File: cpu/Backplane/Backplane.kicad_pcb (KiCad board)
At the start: 2 copper layers, 162 parts, among them J1 GPR A1, J10 SI 2, J11 DI 1, J12 DI 2, J13 SP 1, J14 SP 2, J15 PC 1, J16 PC 2, J17 HOLDING 1, J18 HOLDING 2, J2 GPR A2, J3 GPR B1, J4 GPR B2, J5 GPR C1, J6 GPR C2, J7 GPR D1, J8 GPR D2, J9 SI 1, U1 74LS245, U2 74LS245, U3 74LS245, U4 74LS245, U5 74LS245, U6 74LS245, U7 74LS245, U8 74LS245

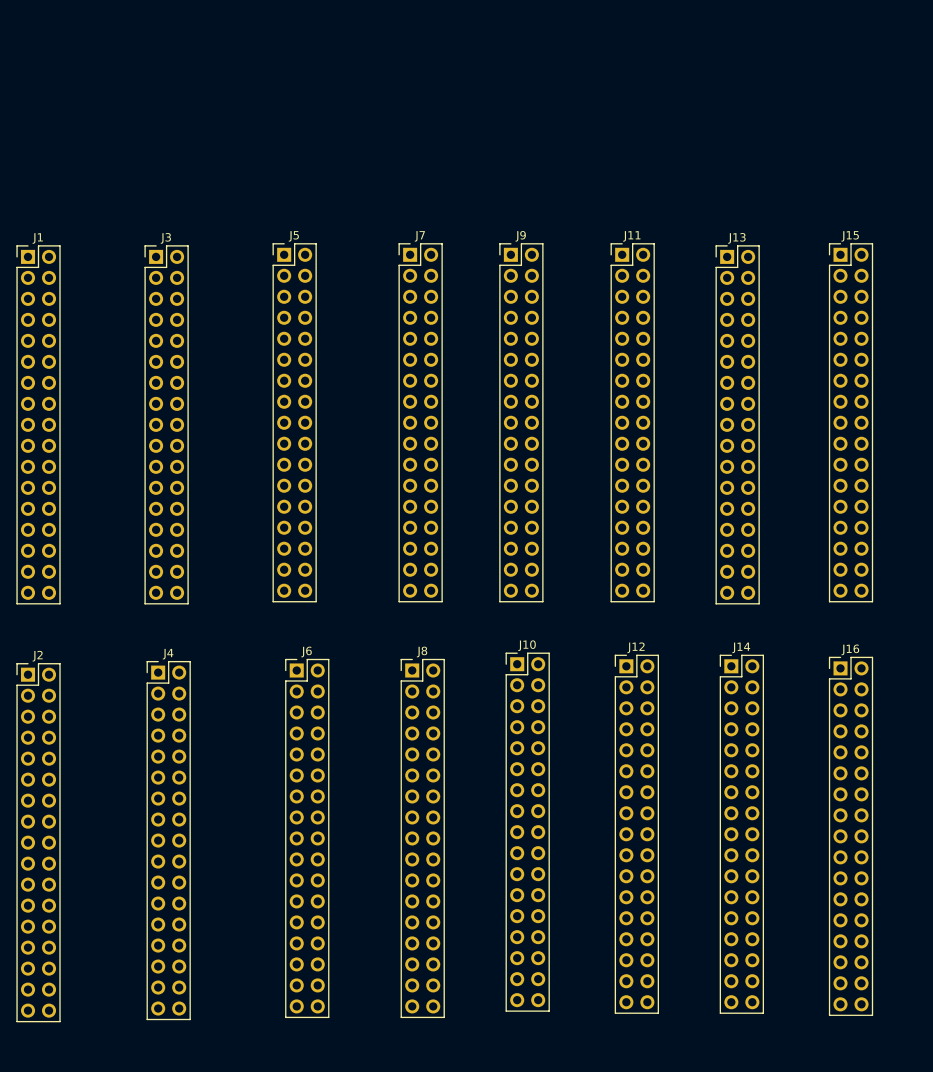
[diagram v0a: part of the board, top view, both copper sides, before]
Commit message: Added missing power pins to GPR
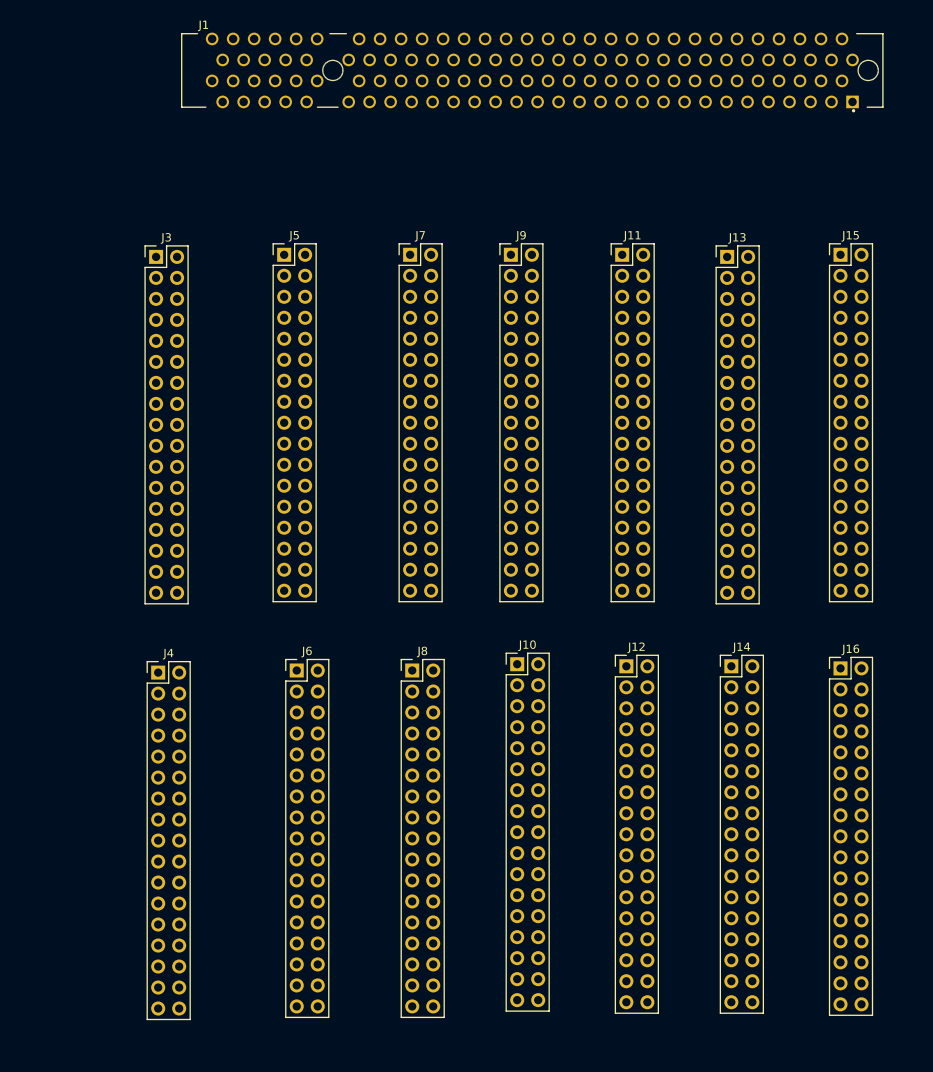
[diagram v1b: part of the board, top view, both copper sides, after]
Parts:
- removed J2: GPR A2, Connector_PinHeader_2.54mm:PinHeader_2x17_P2.54mm_Vertical
- J1: value GPR A1 -> GPR_A; footprint Connector_PinHeader_2.54mm:PinHeader_2x17_P2.54mm_Vertical -> TE-PCI-32bit:TE_1-5145154-2
- moved J1 65.1 mm to (88.7, 0.30)
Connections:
- J1 pad 1: /d_bus_read_gpr_a -> (no net)
- J1 pad 10: /d_bus_04 -> (no net)
- J1 pad 11: Net-(J1-Pad11) -> (no net)
- J1 pad 12: /d_bus_05 -> (no net)
- J1 pad 13: Net-(J1-Pad13) -> (no net)
- J1 pad 14: /d_bus_06 -> (no net)
- J1 pad 15: Net-(J1-Pad15) -> (no net)
- J1 pad 16: /d_bus_07 -> (no net)
- J1 pad 17: Net-(J1-Pad17) -> (no net)
- J1 pad 18: /d_bus_08 -> (no net)
- J1 pad 19: Net-(J1-Pad19) -> (no net)
- J1 pad 2: /d_bus_00 -> (no net)
- J1 pad 20: /d_bus_09 -> (no net)
- J1 pad 21: Net-(J1-Pad21) -> (no net)
- J1 pad 22: /d_bus_10 -> (no net)
- J1 pad 23: /RST -> (no net)
- J1 pad 24: /d_bus_11 -> (no net)
- J1 pad 25: /DBG -> (no net)
- J1 pad 26: /d_bus_12 -> (no net)
- J1 pad 27: /HLT -> (no net)
- J1 pad 28: /d_bus_13 -> (no net)
- J1 pad 29: /~CLK -> (no net)
- J1 pad 3: /d_bus_write_gpr_a -> (no net)
- J1 pad 30: /d_bus_14 -> (no net)
- J1 pad 31: /CLK -> (no net)
- J1 pad 32: /d_bus_15 -> (no net)
- J1 pad 33: GND -> (no net)
- J1 pad 34: +5V -> (no net)
- J1 pad 4: /d_bus_01 -> (no net)
- J1 pad 5: /x_bus_write_gpr_a -> (no net)
- J1 pad 6: /d_bus_02 -> (no net)
- J1 pad 7: /y_bus_write_gpr_a -> (no net)
- J1 pad 8: /d_bus_03 -> (no net)
- J1 pad 9: Net-(J1-Pad9) -> (no net)
- J11 pad 25: /DBG -> /~DBG
- J13 pad 25: /DBG -> /~DBG
- J15 pad 25: /DBG -> /~DBG
- J3 pad 25: /DBG -> /~DBG
- J5 pad 25: /DBG -> /~DBG
- J7 pad 25: /DBG -> /~DBG
- J9 pad 25: /DBG -> /~DBG
- U1 pad 19: /DBG -> /~DBG
- U2 pad 19: /DBG -> /~DBG
- U3 pad 19: /DBG -> /~DBG
- U4 pad 19: /DBG -> /~DBG
- U5 pad 19: /DBG -> /~DBG
- U6 pad 19: /DBG -> /~DBG
- U7 pad 19: /DBG -> /~DBG
- U8 pad 19: /DBG -> /~DBG

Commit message: Upgrade to KiCad 6 and commit a bunch of random stuff
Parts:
- removed R0, R1, R10, R11, R12, R13, R14, R15, R16, R17, R18, R19, R2, R20, R21, R22, R23, R24, R25, R26, R27, R28, R29, R3, R30, R31, R32, R33, R34, R35, R36, R37, R38, R39, R4, R40, R41, R42, R43, R44, R45, R46, R47, R48, R49, R5, R50, R51, R52, R53, R54, R55, R56, R57, R58, R59, R6, R60, R61, R62, R63, R7, R8, R9: 220R, Resistor_SMD:R_0603_1608Metric_Pad1.05x0.95mm_HandSolder
- added C10: 47uF, Capacitor_SMD:CP_Elec_4x5.4, F.Cu at (193.0, 191.2)
- added C11: 47uF, Capacitor_SMD:CP_Elec_4x5.4, F.Cu at (193.0, 171.0)
- added C12: 47uF, Capacitor_SMD:CP_Elec_4x5.4, F.Cu at (193.0, 151.0)
- added C13: 47uF, Capacitor_SMD:CP_Elec_4x5.4, F.Cu at (193.0, 131.0)
- added C14: 47uF, Capacitor_SMD:CP_Elec_4x5.4, F.Cu at (193.0, 111.0)
- added C15: 47uF, Capacitor_SMD:CP_Elec_4x5.4, F.Cu at (193.0, 91.0)
- added C16: 47uF, Capacitor_SMD:CP_Elec_4x5.4, F.Cu at (193.0, 71.0)
- added C17: 47uF, Capacitor_SMD:CP_Elec_4x5.4, F.Cu at (193.0, 51.0)
- added C18: 47uF, Capacitor_SMD:CP_Elec_4x5.4, F.Cu at (62.5, 191.0)
- added C19: 47uF, Capacitor_SMD:CP_Elec_4x5.4, F.Cu at (62.5, 171.0)
- added C20: 47uF, Capacitor_SMD:CP_Elec_4x5.4, F.Cu at (62.5, 151.0)
- added C21: 47uF, Capacitor_SMD:CP_Elec_4x5.4, F.Cu at (62.5, 111.0)
- added C22: 47uF, Capacitor_SMD:CP_Elec_4x5.4, F.Cu at (62.5, 91.0)
- added C23: 47uF, Capacitor_SMD:CP_Elec_4x5.4, F.Cu at (62.5, 71.0)
- added C24: 47uF, Capacitor_SMD:CP_Elec_4x5.4, F.Cu at (62.5, 51.0)
- added C25: 47uF, Capacitor_SMD:CP_Elec_4x5.4, F.Cu at (70.5, 36.1)
- added C9: 0.1uF, Capacitor_SMD:C_0603_1608Metric_Pad1.05x0.95mm_HandSolder, F.Cu at (83.2, 28.4)
- added D64: D_Zener, Diode_THT:D_A-405_P10.16mm_Horizontal, F.Cu at (75.3, 37.4)
- added J19: Conn_01x04_Female, Connector_PinHeader_2.54mm:PinHeader_1x04_P2.54mm_Vertical, F.Cu at (213.3, 28.4)
- added J2: GPR_B, TE-PCI-32bit:TE_1-5145154-2, F.Cu at (241.4, 171.1)
- added J20: Conn_01x07_Female, Connector_PinHeader_2.54mm:PinHeader_1x07_P2.54mm_Vertical, F.Cu at (194.6, 28.4)
- added J21: Conn_01x07_Female, Connector_PinHeader_2.54mm:PinHeader_1x07_P2.54mm_Vertical, F.Cu at (168.2, 28.4)
- added J22: Conn_01x07_Female, Connector_PinHeader_2.54mm:PinHeader_1x07_P2.54mm_Vertical, F.Cu at (141.9, 28.4)
- added J23: Conn_01x07_Female, Connector_PinHeader_2.54mm:PinHeader_1x07_P2.54mm_Vertical, F.Cu at (115.5, 28.4)
- added J24: Conn_01x05_Female, Connector_PinHeader_2.54mm:PinHeader_1x05_P2.54mm_Vertical, F.Cu at (36.0, 199.9)
- added J25: Barrel_Jack, digikey-footprints:Barrel_Jack_5.5mmODx2.1mmID_PJ-202A, F.Cu at (62.5, 36.4)
- added J27: Conn_01x04_Female, Connector_PinHeader_2.54mm:PinHeader_1x04_P2.54mm_Vertical, F.Cu at (36.0, 154.7)
- added J28: Conn_01x14_Female, Connector_PinHeader_2.54mm:PinHeader_1x14_P2.54mm_Vertical, F.Cu at (36.0, 193.7)
- added J29: IO_1, TE-PCI-32bit:TE_1-5145154-2, F.Cu at (111.0, 111.1)
- added J30: IO_2, TE-PCI-32bit:TE_1-5145154-2, F.Cu at (111.0, 91.1)
- added J31: IO_3, TE-PCI-32bit:TE_1-5145154-2, F.Cu at (111.0, 71.1)
- added J32: IO_4, TE-PCI-32bit:TE_1-5145154-2, F.Cu at (111.0, 51.1)
- added RN1: 220R, Resistor_SMD:R_Array_Convex_8x0602, F.Cu at (88.3, 247.5)
- added RN2: 220R, Resistor_SMD:R_Array_Convex_8x0602, F.Cu at (50.7, 245.6)
- added RN3: 220R, Resistor_SMD:R_Array_Convex_8x0602, F.Cu at (217.9, 249.1)
- added RN4: 220R, Resistor_SMD:R_Array_Convex_8x0602, F.Cu at (187.7, 249.1)
- added RN5: 220R, Resistor_SMD:R_Array_Convex_8x0602, F.Cu at (282.1, 248.7)
- added RN6: 220R, Resistor_SMD:R_Array_Convex_8x0602, F.Cu at (250.3, 248.7)
- added RN7: 220R, Resistor_SMD:R_Array_Convex_8x0602, F.Cu at (154.3, 248.7)
- added RN8: 220R, Resistor_SMD:R_Array_Convex_8x0602, F.Cu at (122.0, 248.4)
- added U10: 74LS04, Package_SO:SOIC-14_3.9x8.7mm_P1.27mm, F.Cu at (81.6, 34.0)
- added U9: MCP100-450D, digikey-footprints:SOT-23-3, F.Cu at (70.5, 28.3)
- J10: value SI 2 -> ALU; footprint Connector_PinHeader_2.54mm:PinHeader_2x17_P2.54mm_Vertical -> TE-PCI-32bit:TE_1-5145154-2
- J11: value DI 1 -> Memory; footprint Connector_PinHeader_2.54mm:PinHeader_2x17_P2.54mm_Vertical -> TE-PCI-32bit:TE_1-5145154-2
- J12: value DI 2 -> Conn_01x16_Female; footprint Connector_PinHeader_2.54mm:PinHeader_2x17_P2.54mm_Vertical -> Connector_PinHeader_2.54mm:PinHeader_1x16_P2.54mm_Vertical
- J13: value SP 1 -> Conn_01x16_Female; footprint Connector_PinHeader_2.54mm:PinHeader_2x17_P2.54mm_Vertical -> Connector_PinHeader_2.54mm:PinHeader_1x16_P2.54mm_Vertical
- J14: value SP 2 -> Conn_01x16_Female; footprint Connector_PinHeader_2.54mm:PinHeader_2x17_P2.54mm_Vertical -> Connector_PinHeader_2.54mm:PinHeader_1x16_P2.54mm_Vertical
- J15: value PC 1 -> Conn_01x16_Female; footprint Connector_PinHeader_2.54mm:PinHeader_2x17_P2.54mm_Vertical -> Connector_PinHeader_2.54mm:PinHeader_1x16_P2.54mm_Vertical
- J16: value PC 2 -> Conn_01x04_Female; footprint Connector_PinHeader_2.54mm:PinHeader_2x17_P2.54mm_Vertical -> Connector_PinHeader_2.54mm:PinHeader_1x04_P2.54mm_Vertical
- J17: value HOLDING 1 -> Conn_01x04_Female; footprint Connector_PinHeader_2.54mm:PinHeader_2x17_P2.54mm_Vertical -> Connector_PinHeader_2.54mm:PinHeader_1x04_P2.54mm_Vertical
- J18: value HOLDING 2 -> Conn_01x04_Female; footprint Connector_PinHeader_2.54mm:PinHeader_2x17_P2.54mm_Vertical -> Connector_PinHeader_2.54mm:PinHeader_1x04_P2.54mm_Vertical
- J3: value GPR B1 -> GPR_C; footprint Connector_PinHeader_2.54mm:PinHeader_2x17_P2.54mm_Vertical -> TE-PCI-32bit:TE_1-5145154-2
- J4: value GPR B2 -> GPR_D; footprint Connector_PinHeader_2.54mm:PinHeader_2x17_P2.54mm_Vertical -> TE-PCI-32bit:TE_1-5145154-2
- J5: value GPR C1 -> AReg_PC; footprint Connector_PinHeader_2.54mm:PinHeader_2x17_P2.54mm_Vertical -> TE-PCI-32bit:TE_1-5145154-2
- J6: value GPR C2 -> AReg_SP; footprint Connector_PinHeader_2.54mm:PinHeader_2x17_P2.54mm_Vertical -> TE-PCI-32bit:TE_1-5145154-2
- J7: value GPR D1 -> AReg_SI; footprint Connector_PinHeader_2.54mm:PinHeader_2x17_P2.54mm_Vertical -> TE-PCI-32bit:TE_1-5145154-2
- J8: value GPR D2 -> AReg_DI; footprint Connector_PinHeader_2.54mm:PinHeader_2x17_P2.54mm_Vertical -> TE-PCI-32bit:TE_1-5145154-2
- J9: value SI 1 -> Pipeline; footprint Connector_PinHeader_2.54mm:PinHeader_2x17_P2.54mm_Vertical -> TE-PCI-32bit:TE_1-5145154-2
- moved D15 290.5 mm to (45.9, 254.7)
- moved D14 290.0 mm to (49.7, 254.7)
- moved D13 289.4 mm to (53.5, 254.7)
- moved D12 288.9 mm to (57.3, 254.7)
- moved D11 288.4 mm to (61.1, 254.7)
- moved D10 287.9 mm to (64.9, 254.7)
- moved D9 287.4 mm to (68.7, 254.7)
- moved D8 286.8 mm to (72.5, 254.7)
- moved U1 286.4 mm to (86.5, 238.9)
- moved D7 286.3 mm to (76.3, 254.7)
- moved D6 285.8 mm to (80.1, 254.7)
- moved U2 285.7 mm to (61.5, 238.9)
- moved D5 285.3 mm to (83.9, 254.7)
- moved D4 284.8 mm to (87.7, 254.7)
- moved D3 284.3 mm to (91.5, 254.7)
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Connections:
- D0 pad 1: Net-(D0-Pad1) -> GND
- D1 pad 1: Net-(D1-Pad1) -> GND
- D10 pad 1: Net-(D10-Pad1) -> GND
- D11 pad 1: Net-(D11-Pad1) -> GND
- D12 pad 1: Net-(D12-Pad1) -> GND
- D13 pad 1: Net-(D13-Pad1) -> GND
- D14 pad 1: Net-(D14-Pad1) -> GND
- D15 pad 1: Net-(D15-Pad1) -> GND
- D16 pad 1: Net-(D16-Pad1) -> GND
- D17 pad 1: Net-(D17-Pad1) -> GND
- D18 pad 1: Net-(D18-Pad1) -> GND
- D19 pad 1: Net-(D19-Pad1) -> GND
- D2 pad 1: Net-(D2-Pad1) -> GND
- D20 pad 1: Net-(D20-Pad1) -> GND
- D21 pad 1: Net-(D21-Pad1) -> GND
- D22 pad 1: Net-(D22-Pad1) -> GND
- D23 pad 1: Net-(D23-Pad1) -> GND
- D24 pad 1: Net-(D24-Pad1) -> GND
- D25 pad 1: Net-(D25-Pad1) -> GND
- D26 pad 1: Net-(D26-Pad1) -> GND
- D27 pad 1: Net-(D27-Pad1) -> GND
- D28 pad 1: Net-(D28-Pad1) -> GND
- D29 pad 1: Net-(D29-Pad1) -> GND
- D3 pad 1: Net-(D3-Pad1) -> GND
- D30 pad 1: Net-(D30-Pad1) -> GND
- D31 pad 1: Net-(D31-Pad1) -> GND
- D32 pad 1: Net-(D32-Pad1) -> GND
- D33 pad 1: Net-(D33-Pad1) -> GND
- D34 pad 1: Net-(D34-Pad1) -> GND
- D35 pad 1: Net-(D35-Pad1) -> GND
- D36 pad 1: Net-(D36-Pad1) -> GND
- D37 pad 1: Net-(D37-Pad1) -> GND
- D38 pad 1: Net-(D38-Pad1) -> GND
- D39 pad 1: Net-(D39-Pad1) -> GND
- D4 pad 1: Net-(D4-Pad1) -> GND
- D40 pad 1: Net-(D40-Pad1) -> GND
- D41 pad 1: Net-(D41-Pad1) -> GND
- D42 pad 1: Net-(D42-Pad1) -> GND
- D43 pad 1: Net-(D43-Pad1) -> GND
- D44 pad 1: Net-(D44-Pad1) -> GND
- D45 pad 1: Net-(D45-Pad1) -> GND
- D46 pad 1: Net-(D46-Pad1) -> GND
- D47 pad 1: Net-(D47-Pad1) -> GND
- D48 pad 1: Net-(D48-Pad1) -> GND
- D49 pad 1: Net-(D49-Pad1) -> GND
- D5 pad 1: Net-(D5-Pad1) -> GND
- D50 pad 1: Net-(D50-Pad1) -> GND
- D51 pad 1: Net-(D51-Pad1) -> GND
- D52 pad 1: Net-(D52-Pad1) -> GND
- D53 pad 1: Net-(D53-Pad1) -> GND
- D54 pad 1: Net-(D54-Pad1) -> GND
- D55 pad 1: Net-(D55-Pad1) -> GND
- D56 pad 1: Net-(D56-Pad1) -> GND
- D57 pad 1: Net-(D57-Pad1) -> GND
- D58 pad 1: Net-(D58-Pad1) -> GND
- D59 pad 1: Net-(D59-Pad1) -> GND
- D6 pad 1: Net-(D6-Pad1) -> GND
- D60 pad 1: Net-(D60-Pad1) -> GND
- D61 pad 1: Net-(D61-Pad1) -> GND
- D62 pad 1: Net-(D62-Pad1) -> GND
- D63 pad 1: Net-(D63-Pad1) -> GND
- D7 pad 1: Net-(D7-Pad1) -> GND
- D8 pad 1: Net-(D8-Pad1) -> GND
- D9 pad 1: Net-(D9-Pad1) -> GND
- J12 pad 1: Net-(J12-Pad1) -> /d_bus_00
- J12 pad 10: /a_bus_04 -> /d_bus_09
- J12 pad 11: Net-(J12-Pad11) -> /d_bus_10
- J12 pad 12: /a_bus_05 -> /d_bus_11
- J12 pad 13: Net-(J12-Pad13) -> /d_bus_12
- J12 pad 14: /a_bus_06 -> /d_bus_13
- J12 pad 15: Net-(J12-Pad15) -> /d_bus_14
- J12 pad 16: /a_bus_07 -> /d_bus_15
- J12 pad 2: /a_bus_00 -> /d_bus_01
- J12 pad 3: Net-(J12-Pad3) -> /d_bus_02
- J12 pad 4: /a_bus_01 -> /d_bus_03
- J12 pad 5: Net-(J12-Pad5) -> /d_bus_04
- J12 pad 6: /a_bus_02 -> /d_bus_05
- J12 pad 7: Net-(J12-Pad7) -> /d_bus_06
- J12 pad 8: /a_bus_03 -> /d_bus_07
- J12 pad 9: Net-(J12-Pad9) -> /d_bus_08
- J13 pad 1: /d_bus_read_pc -> /x_bus_00
- J13 pad 10: /d_bus_04 -> /x_bus_09
- J13 pad 11: /reg_carry_sp -> /x_bus_10
- J13 pad 12: /d_bus_05 -> /x_bus_11
- J13 pad 13: /reg_borrow_sp -> /x_bus_12
- J13 pad 14: /d_bus_06 -> /x_bus_13
- J13 pad 15: Net-(J13-Pad15) -> /x_bus_14
- J13 pad 16: /d_bus_07 -> /x_bus_15
- J13 pad 2: /d_bus_00 -> /x_bus_01
- J13 pad 3: /d_bus_write_pc -> /x_bus_02
- J13 pad 4: /d_bus_01 -> /x_bus_03
- J13 pad 5: /a_bus_write_pc -> /x_bus_04
- J13 pad 6: /d_bus_02 -> /x_bus_05
- J13 pad 7: /reg_inc_pc -> /x_bus_06
- J13 pad 8: /d_bus_03 -> /x_bus_07
- J13 pad 9: /reg_dec_pc -> /x_bus_08
- J14 pad 1: Net-(J14-Pad1) -> /y_bus_00
- J14 pad 10: /a_bus_04 -> /y_bus_09
- J14 pad 11: Net-(J14-Pad11) -> /y_bus_10
- J14 pad 12: /a_bus_05 -> /y_bus_11
- J14 pad 13: Net-(J14-Pad13) -> /y_bus_12
- J14 pad 14: /a_bus_06 -> /y_bus_13
- J14 pad 15: Net-(J14-Pad15) -> /y_bus_14
- J14 pad 16: /a_bus_07 -> /y_bus_15
- J14 pad 2: /a_bus_00 -> /y_bus_01
- J14 pad 3: Net-(J14-Pad3) -> /y_bus_02
- J14 pad 4: /a_bus_01 -> /y_bus_03
- J14 pad 5: Net-(J14-Pad5) -> /y_bus_04
- J14 pad 6: /a_bus_02 -> /y_bus_05
- J14 pad 7: Net-(J14-Pad7) -> /y_bus_06
- J14 pad 8: /a_bus_03 -> /y_bus_07
- J14 pad 9: Net-(J14-Pad9) -> /y_bus_08
- J15 pad 1: /d_bus_read_pc -> /a_bus_00
- J15 pad 10: /d_bus_04 -> /a_bus_09
- J15 pad 11: /reg_carry_pc -> /a_bus_10
- J15 pad 12: /d_bus_05 -> /a_bus_11
- J15 pad 13: /reg_borrow_pc -> /a_bus_12
- J15 pad 14: /d_bus_06 -> /a_bus_13
- J15 pad 15: Net-(J15-Pad15) -> /a_bus_14
- J15 pad 16: /d_bus_07 -> /a_bus_15
- J15 pad 2: /d_bus_00 -> /a_bus_01
- J15 pad 3: /d_bus_write_pc -> /a_bus_02
- J15 pad 4: /d_bus_01 -> /a_bus_03
- J15 pad 5: /a_bus_write_pc -> /a_bus_04
- J15 pad 6: /d_bus_02 -> /a_bus_05
- J15 pad 7: /reg_inc_pc -> /a_bus_06
- J15 pad 8: /d_bus_03 -> /a_bus_07
- J15 pad 9: /reg_dec_pc -> /a_bus_08
- J16 pad 1: Net-(J16-Pad1) -> /d_bus_read_gpr_a
- J16 pad 2: /a_bus_00 -> /d_bus_write_gpr_a
- J16 pad 3: Net-(J16-Pad3) -> /x_bus_write_gpr_a
- J16 pad 4: /a_bus_01 -> /y_bus_write_gpr_a
- J17 pad 1: Net-(J17-Pad1) -> /d_bus_read_gpr_b
- J17 pad 2: /d_bus_read_gpr_a -> /d_bus_write_gpr_b
- J17 pad 3: Net-(J17-Pad3) -> /x_bus_write_gpr_b
- J17 pad 4: /d_bus_write_gpr_a -> /y_bus_write_gpr_b
- J18 pad 1: /d_bus_read_pc -> /d_bus_read_gpr_c
- J18 pad 2: /d_bus_read_si -> /d_bus_write_gpr_c
- J18 pad 3: /d_bus_write_pc -> /x_bus_write_gpr_c
- J18 pad 4: /d_bus_write_si -> /y_bus_write_gpr_c
- U1 pad 11: Net-(D7-Pad2) -> Net-(RN1-Pad8)
- U1 pad 12: Net-(D6-Pad2) -> Net-(RN1-Pad7)
- U1 pad 13: Net-(D5-Pad2) -> Net-(RN1-Pad6)
- U1 pad 14: Net-(D4-Pad2) -> Net-(RN1-Pad5)
- U1 pad 15: Net-(D3-Pad2) -> Net-(RN1-Pad4)
- U1 pad 16: Net-(D2-Pad2) -> Net-(RN1-Pad3)
- U1 pad 17: Net-(D1-Pad2) -> Net-(RN1-Pad2)
- U1 pad 18: Net-(D0-Pad2) -> Net-(RN1-Pad1)
- U1 pad 19: /~DBG -> /~{DBG}
- U2 pad 11: Net-(D15-Pad2) -> Net-(RN2-Pad8)
- U2 pad 12: Net-(D14-Pad2) -> Net-(RN2-Pad7)
- U2 pad 13: Net-(D13-Pad2) -> Net-(RN2-Pad6)
- U2 pad 14: Net-(D12-Pad2) -> Net-(RN2-Pad5)
- U2 pad 15: Net-(D11-Pad2) -> Net-(RN2-Pad4)
- U2 pad 16: Net-(D10-Pad2) -> Net-(RN2-Pad3)
- U2 pad 17: Net-(D9-Pad2) -> Net-(RN2-Pad2)
- U2 pad 18: Net-(D8-Pad2) -> Net-(RN2-Pad1)
- U2 pad 19: /~DBG -> /~{DBG}
- U3 pad 11: Net-(D23-Pad2) -> Net-(RN3-Pad8)
- U3 pad 12: Net-(D22-Pad2) -> Net-(RN3-Pad7)
- U3 pad 13: Net-(D21-Pad2) -> Net-(RN3-Pad6)
- U3 pad 14: Net-(D20-Pad2) -> Net-(RN3-Pad5)
- U3 pad 15: Net-(D19-Pad2) -> Net-(RN3-Pad4)
- U3 pad 16: Net-(D18-Pad2) -> Net-(RN3-Pad3)
- U3 pad 17: Net-(D17-Pad2) -> Net-(RN3-Pad2)
- U3 pad 18: Net-(D16-Pad2) -> Net-(RN3-Pad1)
- U3 pad 19: /~DBG -> /~{DBG}
- U4 pad 11: Net-(D31-Pad2) -> Net-(RN4-Pad8)
- U4 pad 12: Net-(D30-Pad2) -> Net-(RN4-Pad7)
- U4 pad 13: Net-(D29-Pad2) -> Net-(RN4-Pad6)
- U4 pad 14: Net-(D28-Pad2) -> Net-(RN4-Pad5)
- U4 pad 15: Net-(D27-Pad2) -> Net-(RN4-Pad4)
- U4 pad 16: Net-(D26-Pad2) -> Net-(RN4-Pad3)
- U4 pad 17: Net-(D25-Pad2) -> Net-(RN4-Pad2)
- U4 pad 18: Net-(D24-Pad2) -> Net-(RN4-Pad1)
- U4 pad 19: /~DBG -> /~{DBG}
- U5 pad 11: Net-(D39-Pad2) -> Net-(RN5-Pad8)
- U5 pad 12: Net-(D38-Pad2) -> Net-(RN5-Pad7)
- U5 pad 13: Net-(D37-Pad2) -> Net-(RN5-Pad6)
- U5 pad 14: Net-(D36-Pad2) -> Net-(RN5-Pad5)
- U5 pad 15: Net-(D35-Pad2) -> Net-(RN5-Pad4)
- U5 pad 16: Net-(D34-Pad2) -> Net-(RN5-Pad3)
- U5 pad 17: Net-(D33-Pad2) -> Net-(RN5-Pad2)
- U5 pad 18: Net-(D32-Pad2) -> Net-(RN5-Pad1)
- U5 pad 19: /~DBG -> /~{DBG}
- U6 pad 11: Net-(D47-Pad2) -> Net-(RN6-Pad8)
- U6 pad 12: Net-(D46-Pad2) -> Net-(RN6-Pad7)
- U6 pad 13: Net-(D45-Pad2) -> Net-(RN6-Pad6)
- U6 pad 14: Net-(D44-Pad2) -> Net-(RN6-Pad5)
- U6 pad 15: Net-(D43-Pad2) -> Net-(RN6-Pad4)
- U6 pad 16: Net-(D42-Pad2) -> Net-(RN6-Pad3)
- U6 pad 17: Net-(D41-Pad2) -> Net-(RN6-Pad2)
- U6 pad 18: Net-(D40-Pad2) -> Net-(RN6-Pad1)
- U6 pad 19: /~DBG -> /~{DBG}
- U7 pad 11: Net-(D55-Pad2) -> Net-(RN7-Pad8)
- U7 pad 12: Net-(D54-Pad2) -> Net-(RN7-Pad7)
- U7 pad 13: Net-(D53-Pad2) -> Net-(RN7-Pad6)
- U7 pad 14: Net-(D52-Pad2) -> Net-(RN7-Pad5)
- U7 pad 15: Net-(D51-Pad2) -> Net-(RN7-Pad4)
- U7 pad 16: Net-(D50-Pad2) -> Net-(RN7-Pad3)
- U7 pad 17: Net-(D49-Pad2) -> Net-(RN7-Pad2)
- U7 pad 18: Net-(D48-Pad2) -> Net-(RN7-Pad1)
- U7 pad 19: /~DBG -> /~{DBG}
- U8 pad 11: Net-(D63-Pad2) -> Net-(RN8-Pad8)
- U8 pad 12: Net-(D62-Pad2) -> Net-(RN8-Pad7)
- U8 pad 13: Net-(D61-Pad2) -> Net-(RN8-Pad6)
- U8 pad 14: Net-(D60-Pad2) -> Net-(RN8-Pad5)
- U8 pad 15: Net-(D59-Pad2) -> Net-(RN8-Pad4)
- U8 pad 16: Net-(D58-Pad2) -> Net-(RN8-Pad3)
- U8 pad 17: Net-(D57-Pad2) -> Net-(RN8-Pad2)
- U8 pad 18: Net-(D56-Pad2) -> Net-(RN8-Pad1)
- U8 pad 19: /~DBG -> /~{DBG}
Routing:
- net +5V: track 0.00 -> 1486.2 mm, vias 0 -> 18
- net /~{DBG}: track 0.00 -> 776.7 mm, vias 0 -> 3
- net /d_bus_15: track 0.00 -> 525.5 mm, vias 0 -> 3
- net /d_bus_14: track 0.00 -> 523.3 mm, vias 0 -> 3
- net /d_bus_13: track 0.00 -> 516.0 mm, vias 0 -> 3
- net /d_bus_12: track 0.00 -> 514.6 mm, vias 0 -> 3
- net /d_bus_11: track 0.00 -> 508.4 mm, vias 0 -> 3
- net /RST: track 0.00 -> 507.4 mm, vias 0 -> 4
- net /d_bus_10: track 0.00 -> 506.5 mm, vias 0 -> 3
- net /d_bus_09: track 0.00 -> 499.5 mm, vias 0 -> 3
- net /d_bus_08: track 0.00 -> 498.0 mm, vias 0 -> 3
- net /~{CLK}: track 0.00 -> 495.8 mm, vias 0 -> 3
- net /CLK: track 0.00 -> 493.2 mm, vias 0 -> 3
- net /HLT: track 0.00 -> 493.0 mm, vias 0 -> 3
- net /d_bus_07: track 0.00 -> 491.5 mm, vias 0 -> 3
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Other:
- board outline added: 268 x 237.9 mm
- net class Default removed
- board text added: "A15 A14 A13 A12 A11 A10 A09 A08 A07 A06 A05 A04 A03 A02 A01 A00"
- board text added: "A_WRT"
- board text added: "Address Bus"
- board text added: "BRW"
- board text added: "CAR"
- board text added: "D15 D14 D13 D12 D11 D10 D09 D08 D07 D06 D05 D04 D03 D02 D01 D00"
- board text added: "DEC"
- board text added: "D_RD"
- board text added: "D_WRT"
- board text added: "Data Bus"
- board text added: "INC"
- board text added: "X Bus"
- board text added: "X15 X14 X13 X12 X11 X10 X09 X08 X07 X06 X05 X04 X03 X02 X01 X00"
- board text added: "Y Bus"
- board text added: "Y15 Y14 Y13 Y12 Y11 Y10 Y09 Y08 Y07 Y06 Y05 Y04 Y03 Y02 Y01 Y00"
